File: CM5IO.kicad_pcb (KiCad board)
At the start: 4 copper layers, 130 x 80 mm, 64 parts, among them J1 Conn_02x06_Top_Bottom, J11 USB_C_Receptacle_USB2.0, J12 USB3_A, J14 JST_SHBM04B-SRSS-TB, J16 Conn_01x22_Female, J22 690-019-298-412, J3 Conn_01x03, J4 Bus_M.2_Socket_M, J5 Conn_01x22_Female, J6 THD-02-R, J8 THD-20-R, J9 THD-02-R, SW1 Right angle Tact button, U1 TPD4EUSB30, U12 RT9742SNGV, U2 TPD4EUSB30, U3 MagJack-A70-112-331N126, U5 74LVC1G07SE-7, U6 AP22653W6, U7 ASEK-32.768KHZ-L-R-T, U8 AP3441SHE-7B

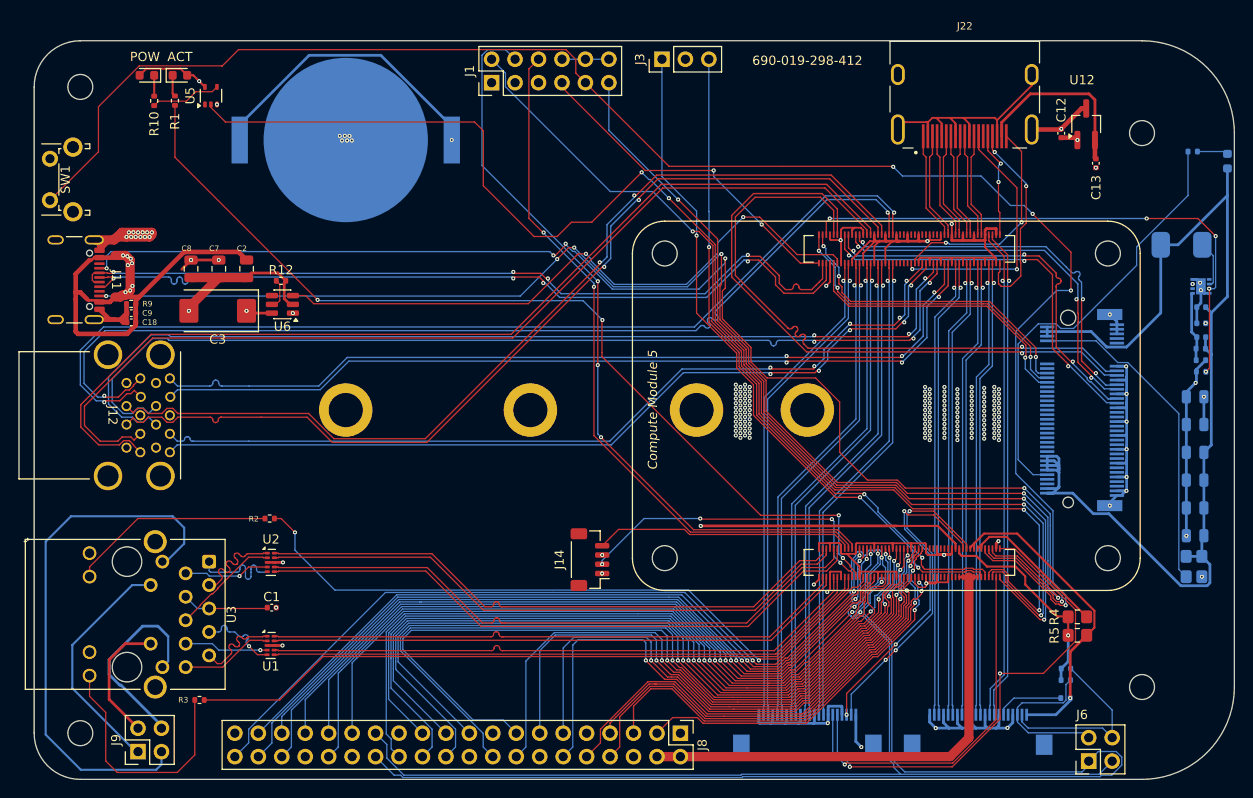
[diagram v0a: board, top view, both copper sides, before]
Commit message: added credentials and GPIO pinout silkscreen graphics, improvements on various stuff
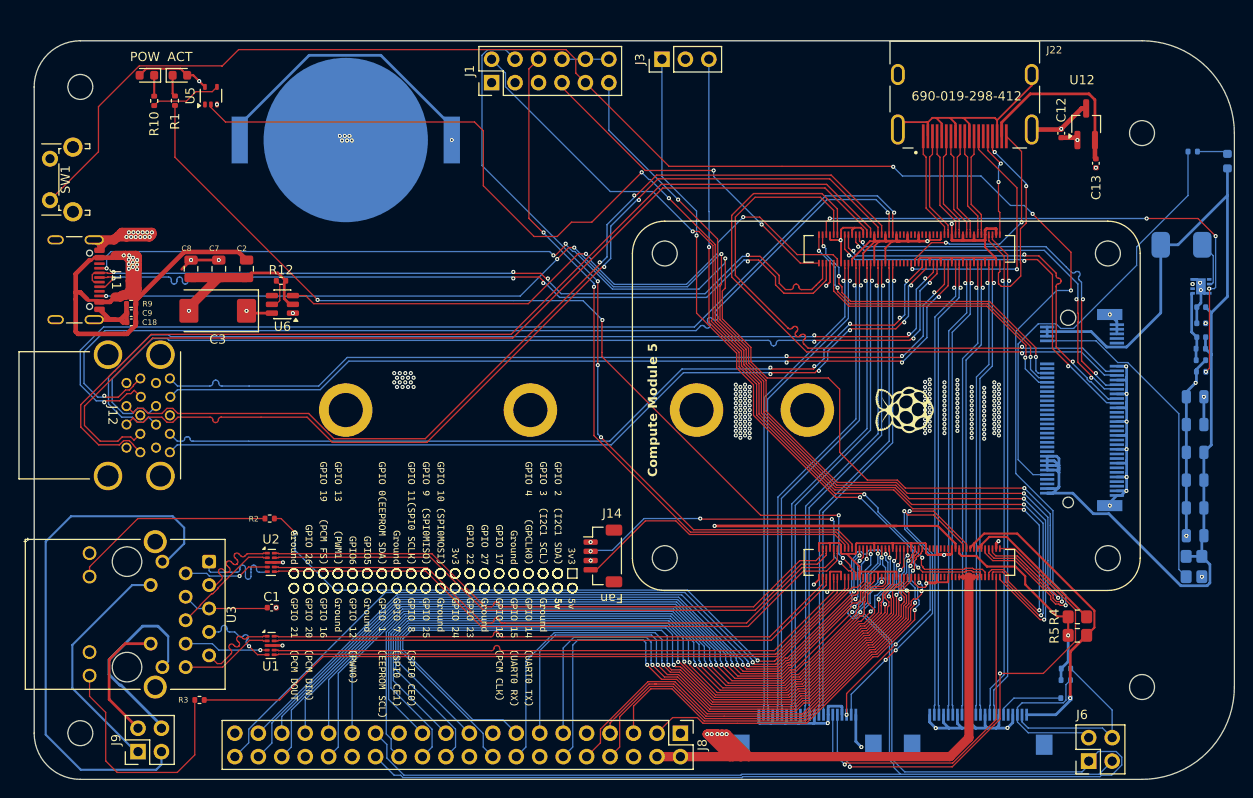
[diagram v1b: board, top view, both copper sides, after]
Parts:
- added logo1: KiCad-Logo2_5mm_SilkScreen, Symbol:KiCad-Logo2_5mm_SilkScreen, B.Cu at (210.8, 115.9)
- moved J14 1.46 mm to (146.6, 105.8), turned to -90 degrees
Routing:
- net /+5v: track 109.1 -> 129.0 mm, vias 14 -> 22
- net /CM5_GPIO ( Ethernet, GPIO, SDCARD)/VBAT: track 114.3 -> 129.8 mm
- net /CM5_GPIO ( Ethernet, GPIO, SDCARD)/TACHO: track 28.1 -> 31.2 mm
- net /CM5_GPIO ( Ethernet, GPIO, SDCARD)/ID_SD: track 126.3 -> 125.0 mm
- net /CC1: track 149.7 -> 150.5 mm
- net GND: vias 195 -> 211
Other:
- board text added: "${PROJ_TIME_DD}/${PROJ_TIME_MM}/${PROJ_TIME_YYYY}"
- board text added: "${PROJ_TIME_YYYY}${PROJ_TIME_MM}${PROJ_ID}${PROJ_REV_MAJOR}${PROJ_REV_MINOR}"
- board text added: "Camera / Display 0"
- board text added: "Camera / Display 1"
- board text added: "Fan"
- board text added: "doruk"
- board text added: "v${PROJ_REV_MAJOR}.${PROJ_REV_MINOR}"
